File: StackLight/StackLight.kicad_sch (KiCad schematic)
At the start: 2 parts, among them J1 RJ45, J2 Conn_01x05

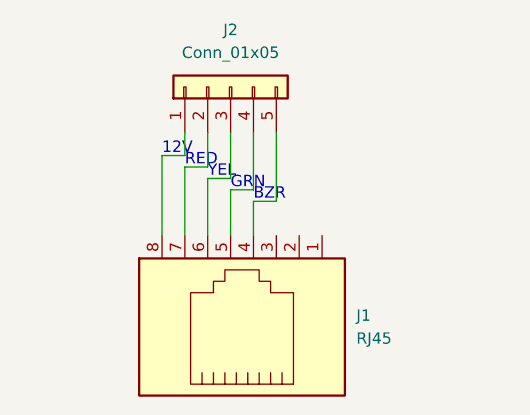
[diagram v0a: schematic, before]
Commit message: Updated Button and Stacklight PCB to not have backwards fucking footprint shit.
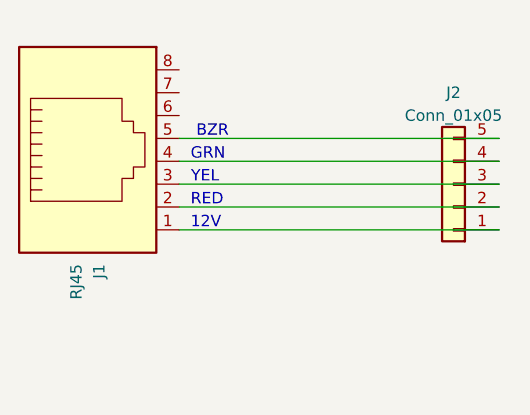
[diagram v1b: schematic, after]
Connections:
- net at J1.1: now also J2.1 (Pin_1)
- net at J1.2: now also J2.2 (Pin_2)
- net at J1.3: now also J2.3 (Pin_3)
- net at J1.4: now also J2.4 (Pin_4); no longer J2.5 (Pin_5)
- net at J1.5: now also J2.5 (Pin_5); no longer J2.4 (Pin_4)
- net at J1.6: no longer J2.3 (Pin_3)
- net at J1.7: no longer J2.2 (Pin_2)
- net at J1.8: no longer J2.1 (Pin_1)
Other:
- moved on the sheet: J1, J2
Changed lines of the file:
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@@
-(kicad_sch (version 20211123) (generator eeschema)
+(kicad_sch (version 20230121) (generator eeschema)
   (paper "A4")
-  (wire (pts (xy 120.65 90.17) (xy 120.65 93.98))
-    (stroke (width 0) (type default) (color 0 0 0 0))
+  (wire (pts (xy 117.475 100.965) (xy 153.035 100.965))
+    (stroke (width 0) (type default))
   )
-  (wire (pts (xy 125.73 90.17) (xy 125.73 96.52))
-    (stroke (width 0) (type default) (color 0 0 0 0))
+  (wire (pts (xy 117.475 98.425) (xy 153.035 98.425))
+    (stroke (width 0) (type default))
   )
-  (wire (pts (xy 118.11 90.17) (xy 118.11 92.71))
-    (stroke (width 0) (type default) (color 0 0 0 0))
+  (wire (pts (xy 117.475 90.805) (xy 153.035 90.805))
+    (stroke (width 0) (type default))
   )
-  (wire (pts (xy 118.11 93.98) (xy 118.11 101.6))
-    (stroke (width 0) (type default) (color 0 0 0 0))
+  (wire (pts (xy 117.475 95.885) (xy 153.035 95.885))
+    (stroke (width 0) (type default))
   )
-  (wire (pts (xy 125.73 101.6) (xy 125.73 97.79))
-    (stroke (width 0) (type default) (color 0 0 0 0))
+  (wire (pts (xy 117.475 93.345) (xy 153.035 93.345))
+    (stroke (width 0) (type default))
   )
-  (wire (pts (xy 128.27 97.79) (xy 128.27 90.17))
-    (stroke (width 0) (type default) (color 0 0 0 0))
-  )
-  (wire (pts (xy 125.73 96.52) (xy 123.19 96.52))
-    (stroke (width 0) (type default) (color 0 0 0 0))
-  )
-  (wire (pts (xy 125.73 97.79) (xy 128.27 97.79))
-    (stroke (width 0) (type default) (color 0 0 0 0))
-  )
-  (wire (pts (xy 120.65 95.25) (xy 123.19 95.25))
-    (stroke (width 0) (type default) (color 0 0 0 0))
-  )
-  (wire (pts (xy 118.11 92.71) (xy 115.57 92.71))
-    (stroke (width 0) (type default) (color 0 0 0 0))
-  )
-  (wire (pts (xy 123.19 95.25) (xy 123.19 90.17))
-    (stroke (width 0) (type default) (color 0 0 0 0))
-  )
-  (wire (pts (xy 120.65 101.6) (xy 120.65 95.25))
-    (stroke (width 0) (type default) (color 0 0 0 0))
-  )
-  (wire (pts (xy 115.57 92.71) (xy 115.57 101.6))
-    (stroke (width 0) (type default) (color 0 0 0 0))
-  )
-  (wire (pts (xy 120.65 93.98) (xy 118.11 93.98))
-    (stroke (width 0) (type default) (color 0 0 0 0))
-  )
-  (wire (pts (xy 123.19 96.52) (xy 123.19 101.6))
-    (stroke (width 0) (type default) (color 0 0 0 0))
-  )
-  (text "GRN" (at 123.19 96.52 0)
+  (text "GRN" (at 118.745 93.345 0)
     (effects (font (size 1.27 1.27)) (justify left bottom))
   )
-  (text "YEL\n" (at 120.65 95.25 0)
+  (text "YEL\n" (at 121.92 95.885 0)
+    (effects (font (size 1.27 1.27)) (justify right bottom))
+  )
+  (text "BZR\n" (at 119.38 90.805 0)
     (effects (font (size 1.27 1.27)) (justify left bottom))
   )
-  (text "BZR\n" (at 125.73 97.79 0)
+  (text "RED\n" (at 118.745 98.425 0)
     (effects (font (size 1.27 1.27)) (justify left bottom))
   )
-  (text "RED\n" (at 118.11 93.98 0)
+  (text "12V\n" (at 118.745 100.965 0)
     (effects (font (size 1.27 1.27)) (justify left bottom))
   )
-  (text "12V\n" (at 115.57 92.71 0)
-    (effects (font (size 1.27 1.27)) (justify left bottom))
-  )
-  (symbol (lib_id "Connector:RJ45") (at 125.73 111.76 90) (unit 1)
-    (in_bom yes) (on_board yes) (fields_autoplaced)
-    (property "Reference" "J1" (id 0) (at 137.16 110.4899 90)
+  (symbol (lib_id "Connector:RJ45") (at 107.315 93.345 0) (unit 1)
+    (in_bom yes) (on_board yes) (dnp no) (fields_autoplaced)
+    (property "Reference" "J1" (at 108.5851 104.775 90)
       (effects (font (size 1.27 1.27)) (justify right))
     )
-    (property "Value" "RJ45" (id 1) (at 137.16 113.0299 90)
+    (property "Value" "RJ45" (at 106.0451 104.775 90)
       (effects (font (size 1.27 1.27)) (justify right))
     )
-    (property "Footprint" "footprints:RCH RC00139" (id 2) (at 125.095 111.76 90)
+    (property "Footprint" "footprints:RCH RC00139" (at 107.315 92.71 90)
       (effects (font (size 1.27 1.27)) hide)
     )
-    (property "Datasheet" "https://lcsc.com/product-detail/Ethernet-Connectors-Modular-Connectors-RJ45-RJ11_RCH-RC00139_C708595.html" (id 3) (at 125.095 111.76 90)
+    (property "Datasheet" "https://lcsc.com/product-detail/Ethernet-Connectors-Modular-Connectors-RJ45-RJ11_RCH-RC00139_C708595.html" (at 107.315 92.71 90)
       (effects (font (size 1.27 1.27)) hide)
     )
@@
     (pin "7")
     (pin "8")
+    (instances
+      (project "StackLight"
+        (path "/37969f5f-fd48-409d-b83c-171d7e3cb961"
+          (reference "J1") (unit 1)
+        )
+      )
+    )
   )
-  (symbol (lib_id "Connector_Generic:Conn_01x05") (at 123.19 85.09 90) (unit 1)
-    (in_bom yes) (on_board yes) (fields_autoplaced)
-    (property "Reference" "J2" (id 0) (at 123.19 78.74 90))
-    (property "Value" "Conn_01x05" (id 1) (at 123.19 81.28 90))
-    (property "Footprint" "Connector_PinHeader_2.54mm:PinHeader_1x05_P2.54mm_Vertical" (id 2) (at 123.19 85.09 0)
+  (symbol (lib_id "Connector_Generic:Conn_01x05") (at 147.955 95.885 180) (unit 1)
+    (in_bom yes) (on_board yes) (dnp no) (fields_autoplaced)
+    (property "Reference" "J2" (at 147.955 85.725 0)
+      (effects (font (size 1.27 1.27)))
+    )
+    (property "Value" "Conn_01x05" (at 147.955 88.265 0)
+      (effects (font (size 1.27 1.27)))
+    )
+    (property "Footprint" "Connector_PinHeader_2.54mm:PinHeader_1x05_P2.54mm_Vertical" (at 147.955 95.885 0)
       (effects (font (size 1.27 1.27)) hide)
     )
-    (property "Datasheet" "~" (id 3) (at 123.19 85.09 0)
+    (property "Datasheet" "~" (at 147.955 95.885 0)
       (effects (font (size 1.27 1.27)) hide)
     )
@@
     (pin "4")
     (pin "5")
+    (instances
+      (project "StackLight"
+        (path "/37969f5f-fd48-409d-b83c-171d7e3cb961"
+          (reference "J2") (unit 1)
+        )
+      )
+    )
   )
   (sheet_instances
     (path "/" (page "1"))
   )
-  (symbol_instances
-    (path "/f6ba5663-2e73-49b5-b71d-c6f2b37e45bd"
-      (reference "J1") (unit 1) (value "RJ45") (footprint "footprints:RCH RC00139")
-    )
-    (path "/f71a21ce-6257-4341-8e5c-d88685c2baf4"
-      (reference "J2") (unit 1) (value "Conn_01x05") (footprint "Connector_PinHeader_2.54mm:PinHeader_1x05_P2.54mm_Vertical")
-    )
-  )
 )

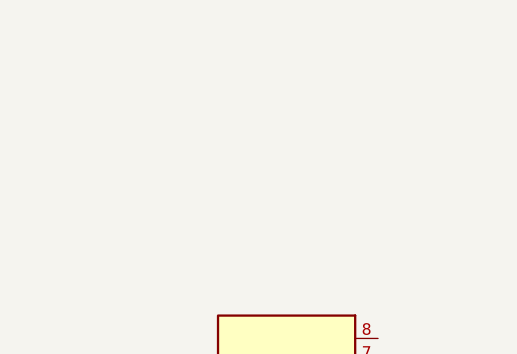
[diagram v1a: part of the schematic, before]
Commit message: Update to non-hole design.  Verify wire gagues.
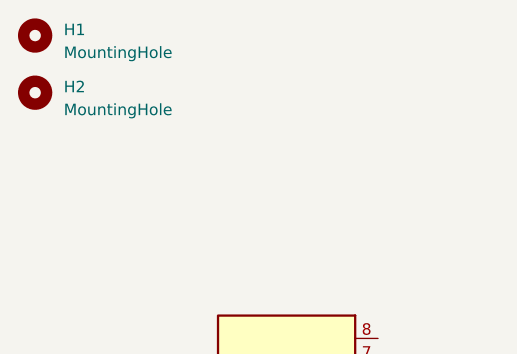
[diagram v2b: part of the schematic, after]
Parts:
- added H1, H2: MountingHole, MountingHole:MountingHole_3.2mm_M3, symbol Mechanical:MountingHole
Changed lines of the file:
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@@
     (effects (font (size 1.27 1.27)) (justify left bottom))
+  )
+  (symbol (lib_id "Mechanical:MountingHole") (at 79.375 49.53 0) (unit 1)
+    (in_bom yes) (on_board yes) (dnp no) (fields_autoplaced)
+    (property "Reference" "H1" (at 82.55 48.895 0)
+      (effects (font (size 1.27 1.27)) (justify left))
+    )
+    (property "Value" "MountingHole" (at 82.55 51.435 0)
+      (effects (font (size 1.27 1.27)) (justify left))
+    )
+    (property "Footprint" "MountingHole:MountingHole_3.2mm_M3" (at 79.375 49.53 0)
+      (effects (font (size 1.27 1.27)) hide)
+    )
+    (property "Datasheet" "~" (at 79.375 49.53 0)
+      (effects (font (size 1.27 1.27)) hide)
+    )
+    (instances
+      (project "StackLight"
+        (path "/37969f5f-fd48-409d-b83c-171d7e3cb961"
+          (reference "H1") (unit 1)
+        )
+      )
+    )
   )
   (symbol (lib_id "Connector:RJ45") (at 107.315 93.345 0) (unit 1)
@@
         )
       )
+    )
+  )
+  (symbol (lib_id "Mechanical:MountingHole") (at 79.375 55.88 0) (unit 1)
+    (in_bom yes) (on_board yes) (dnp no) (fields_autoplaced)
+    (property "Reference" "H2" (at 82.55 55.245 0)
+      (effects (font (size 1.27 1.27)) (justify left))
+    )
+    (property "Value" "MountingHole" (at 82.55 57.785 0)
+      (effects (font (size 1.27 1.27)) (justify left))
+    )
+    (property "Footprint" "MountingHole:MountingHole_3.2mm_M3" (at 79.375 55.88 0)
+      (effects (font (size 1.27 1.27)) hide)
+    )
+    (property "Datasheet" "~" (at 79.375 55.88 0)
+      (effects (font (size 1.27 1.27)) hide)
+    )
+    (instances
+      (project "StackLight"
+        (path "/37969f5f-fd48-409d-b83c-171d7e3cb961"
+          (reference "H2") (unit 1)
+        )
+      )

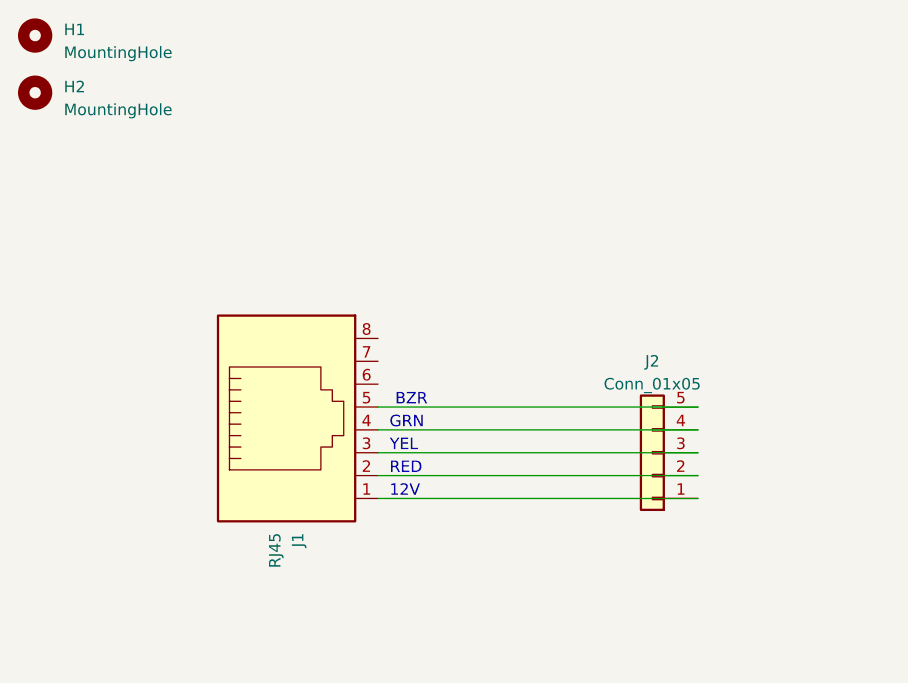
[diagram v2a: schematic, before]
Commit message: Added wire strain relief that should fit.
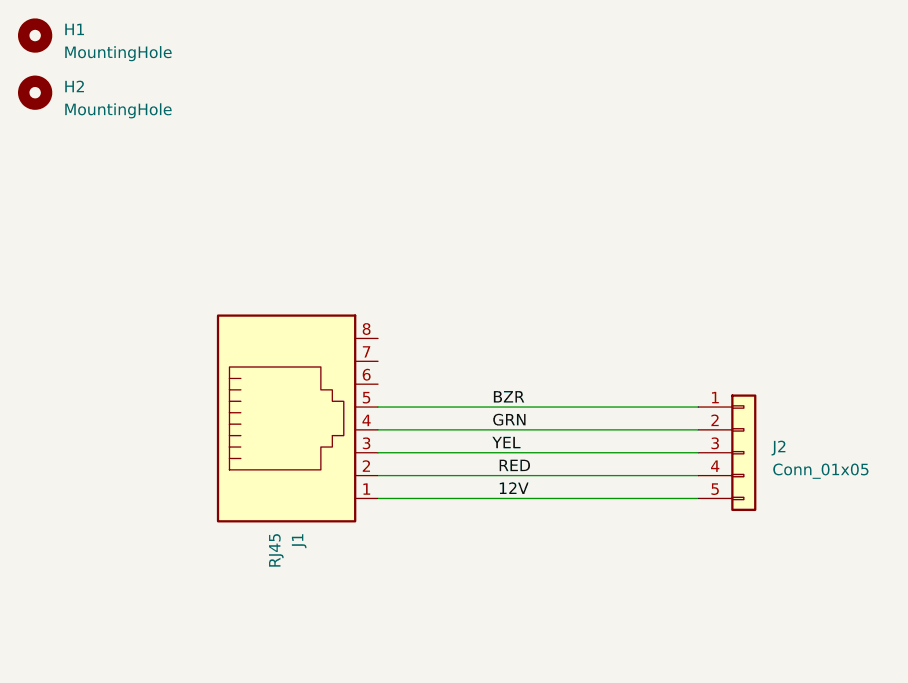
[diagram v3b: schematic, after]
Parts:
- J2: footprint Connector_PinHeader_2.54mm:PinHeader_1x05_P2.54mm_Vertical -> Connector_Wire:SolderWire-0.127sqmm_1x05_P3.7mm_D0.48mm_OD1mm_Relief
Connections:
- net 12V: now reaches J1.1
- net 12V: now also J2.5 (Pin_5); no longer J2.1 (Pin_1)
- net GRN: now reaches J2.2 (Pin_2)
- net GRN: now also J1.4; no longer J1.2
- net YEL: now reaches J1.3, J2.3 (Pin_3)
- net RED: now reaches J2.4 (Pin_4)
- net RED: now also J1.2; no longer J1.4
- net BZR: now reaches J1.5
- net BZR: now also J2.1 (Pin_1); no longer J2.5 (Pin_5)
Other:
- note removed: "12V"
- note removed: "BZR"
- note removed: "GRN"
- note removed: "RED"
- note removed: "YEL"
- moved on the sheet: J2
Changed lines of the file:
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@@
     (stroke (width 0) (type default))
   )
-  (text "GRN" (at 118.745 93.345 0)
+  (label "BZR" (at 130.175 90.805 0) (fields_autoplaced)
     (effects (font (size 1.27 1.27)) (justify left bottom))
   )
-  (text "YEL\n" (at 121.92 95.885 0)
-    (effects (font (size 1.27 1.27)) (justify right bottom))
-  )
-  (text "BZR\n" (at 119.38 90.805 0)
+  (label "12V" (at 130.81 100.965 0) (fields_autoplaced)
     (effects (font (size 1.27 1.27)) (justify left bottom))
   )
-  (text "RED\n" (at 118.745 98.425 0)
+  (label "GRN" (at 130.175 93.345 0) (fields_autoplaced)
     (effects (font (size 1.27 1.27)) (justify left bottom))
   )
-  (text "12V\n" (at 118.745 100.965 0)
+  (label "RED" (at 130.81 98.425 0) (fields_autoplaced)
+    (effects (font (size 1.27 1.27)) (justify left bottom))
+  )
+  (label "YEL" (at 130.175 95.885 0) (fields_autoplaced)
     (effects (font (size 1.27 1.27)) (justify left bottom))
   )
@@
     )
   )
-  (symbol (lib_id "Connector_Generic:Conn_01x05") (at 147.955 95.885 180) (unit 1)
+  (symbol (lib_id "Connector_Generic:Conn_01x05") (at 158.115 95.885 0) (unit 1)
     (in_bom yes) (on_board yes) (dnp no) (fields_autoplaced)
-    (property "Reference" "J2" (at 147.955 85.725 0)
-      (effects (font (size 1.27 1.27)))
+    (property "Reference" "J2" (at 161.29 95.25 0)
+      (effects (font (size 1.27 1.27)) (justify left))
     )
-    (property "Value" "Conn_01x05" (at 147.955 88.265 0)
-      (effects (font (size 1.27 1.27)))
+    (property "Value" "Conn_01x05" (at 161.29 97.79 0)
+      (effects (font (size 1.27 1.27)) (justify left))
     )
-    (property "Footprint" "Connector_PinHeader_2.54mm:PinHeader_1x05_P2.54mm_Vertical" (at 147.955 95.885 0)
+    (property "Footprint" "Connector_Wire:SolderWire-0.127sqmm_1x05_P3.7mm_D0.48mm_OD1mm_Relief" (at 158.115 95.885 0)
       (effects (font (size 1.27 1.27)) hide)
     )
-    (property "Datasheet" "~" (at 147.955 95.885 0)
+    (property "Datasheet" "~" (at 158.115 95.885 0)
       (effects (font (size 1.27 1.27)) hide)
     )

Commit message: Updated PCB revisions, swapped to larger footprint for stacklight connector, release cutting soon.
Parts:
- J2: footprint Connector_Wire:SolderWire-0.127sqmm_1x05_P3.7mm_D0.48mm_OD1mm_Relief -> Connector_Wire:SolderWire-1.5sqmm_1x05_P6mm_D1.7mm_OD3mm_Relief
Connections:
- net GND: now reaches J1.8
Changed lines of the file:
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@@
 (kicad_sch (version 20230121) (generator eeschema)
   (paper "A4")
+  (wire (pts (xy 117.475 83.185) (xy 123.825 83.185))
+    (stroke (width 0) (type default))
+  )
   (wire (pts (xy 117.475 100.965) (xy 153.035 100.965))
     (stroke (width 0) (type default))
@@
     )
   )
+  (symbol (lib_id "power:GND") (at 123.825 83.185 0) (unit 1)
+    (in_bom yes) (on_board yes) (dnp no) (fields_autoplaced)
+    (property "Reference" "#PWR01" (at 123.825 89.535 0)
+      (effects (font (size 1.27 1.27)) hide)
+    )
+    (property "Value" "GND" (at 123.825 87.63 0)
+      (effects (font (size 1.27 1.27)))
+    )
+    (property "Footprint" "" (at 123.825 83.185 0)
+      (effects (font (size 1.27 1.27)) hide)
+    )
+    (property "Datasheet" "" (at 123.825 83.185 0)
+      (effects (font (size 1.27 1.27)) hide)
+    )
+    (pin "1")
+    (instances
+      (project "StackLight"
+        (path "/37969f5f-fd48-409d-b83c-171d7e3cb961"
+          (reference "#PWR01") (unit 1)
+        )
+      )
+    )
+  )
   (symbol (lib_id "Connector:RJ45") (at 107.315 93.345 0) (unit 1)
     (in_bom yes) (on_board yes) (dnp no) (fields_autoplaced)
@@
       (effects (font (size 1.27 1.27)) (justify left))
     )
-    (property "Footprint" "Connector_Wire:SolderWire-0.127sqmm_1x05_P3.7mm_D0.48mm_OD1mm_Relief" (at 158.115 95.885 0)
+    (property "Footprint" "Connector_Wire:SolderWire-1.5sqmm_1x05_P6mm_D1.7mm_OD3mm_Relief" (at 158.115 95.885 0)
       (effects (font (size 1.27 1.27)) hide)
     )
